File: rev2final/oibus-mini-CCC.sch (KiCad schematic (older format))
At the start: 90 parts, among them J1 Conn_01x04_Female, J2 USB_B_Micro, J3 DNP, J4 Conn_01x02_Female, P1 TC2030-MCP, Q1 DMG3415U-7, Q2 NMOS, Q3 NMOS, SW1 SW_Push, SW2 SW_Push, U1 AP2112K-3.3, U10 TPD3E001DRLR, U2 SAM-M8Q, U3 NINA-B311-00B, U4 MCP73831-2-OT, U5 MCP1624T, U6 SHT31-DIS-B, U7 DNP, U8 STM32F303CCTx, U9 DW01C-G, Y1 16M, Y2 32kHz

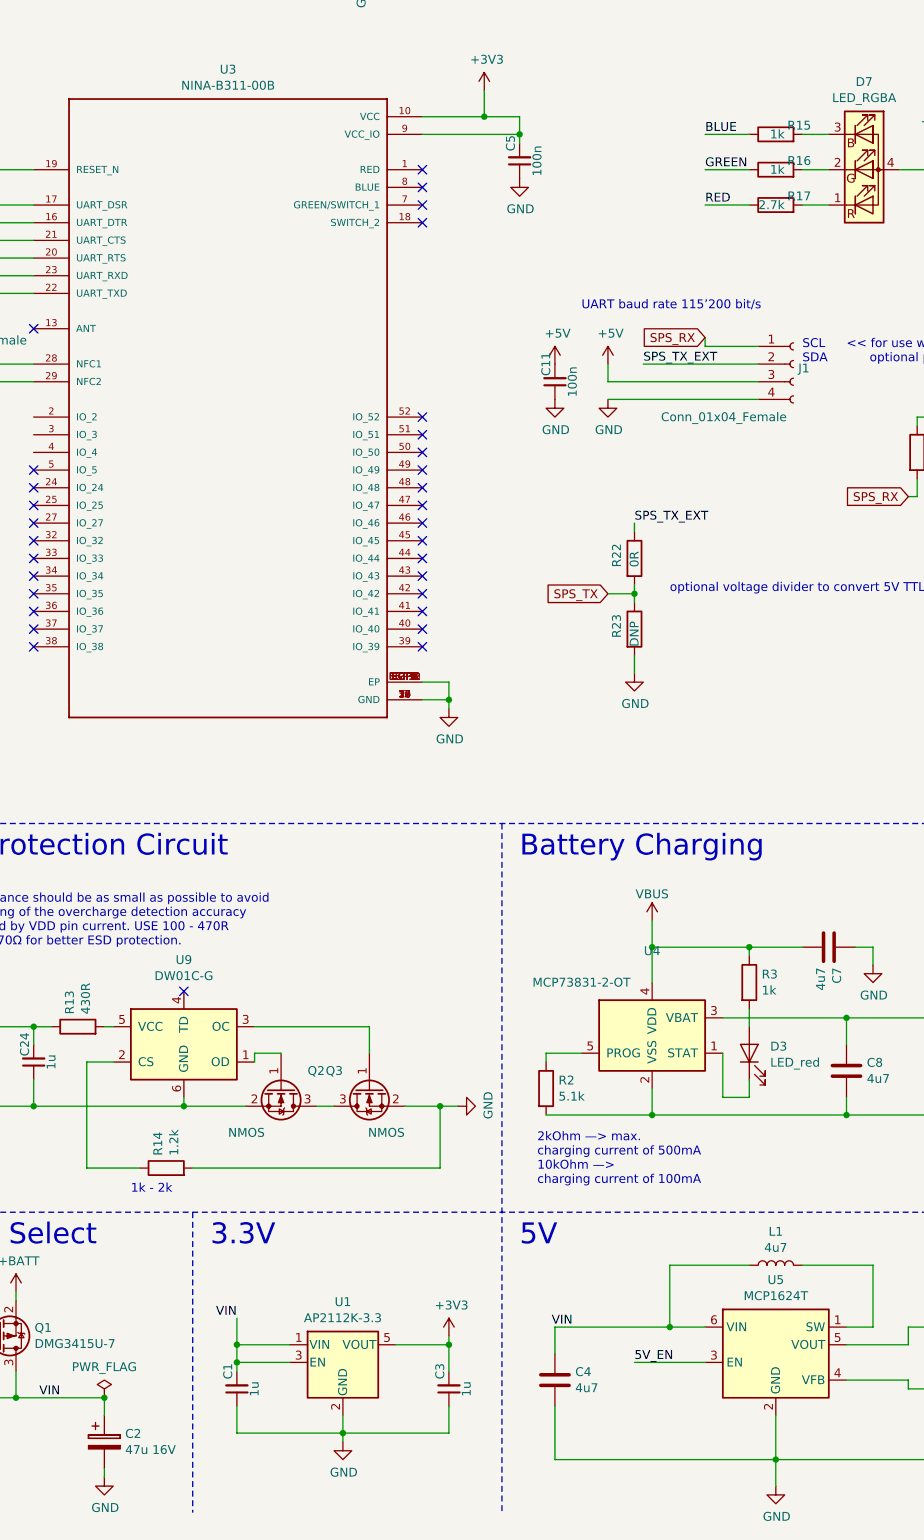
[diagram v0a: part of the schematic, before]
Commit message: Generated final Manufacturing BOM as ordered
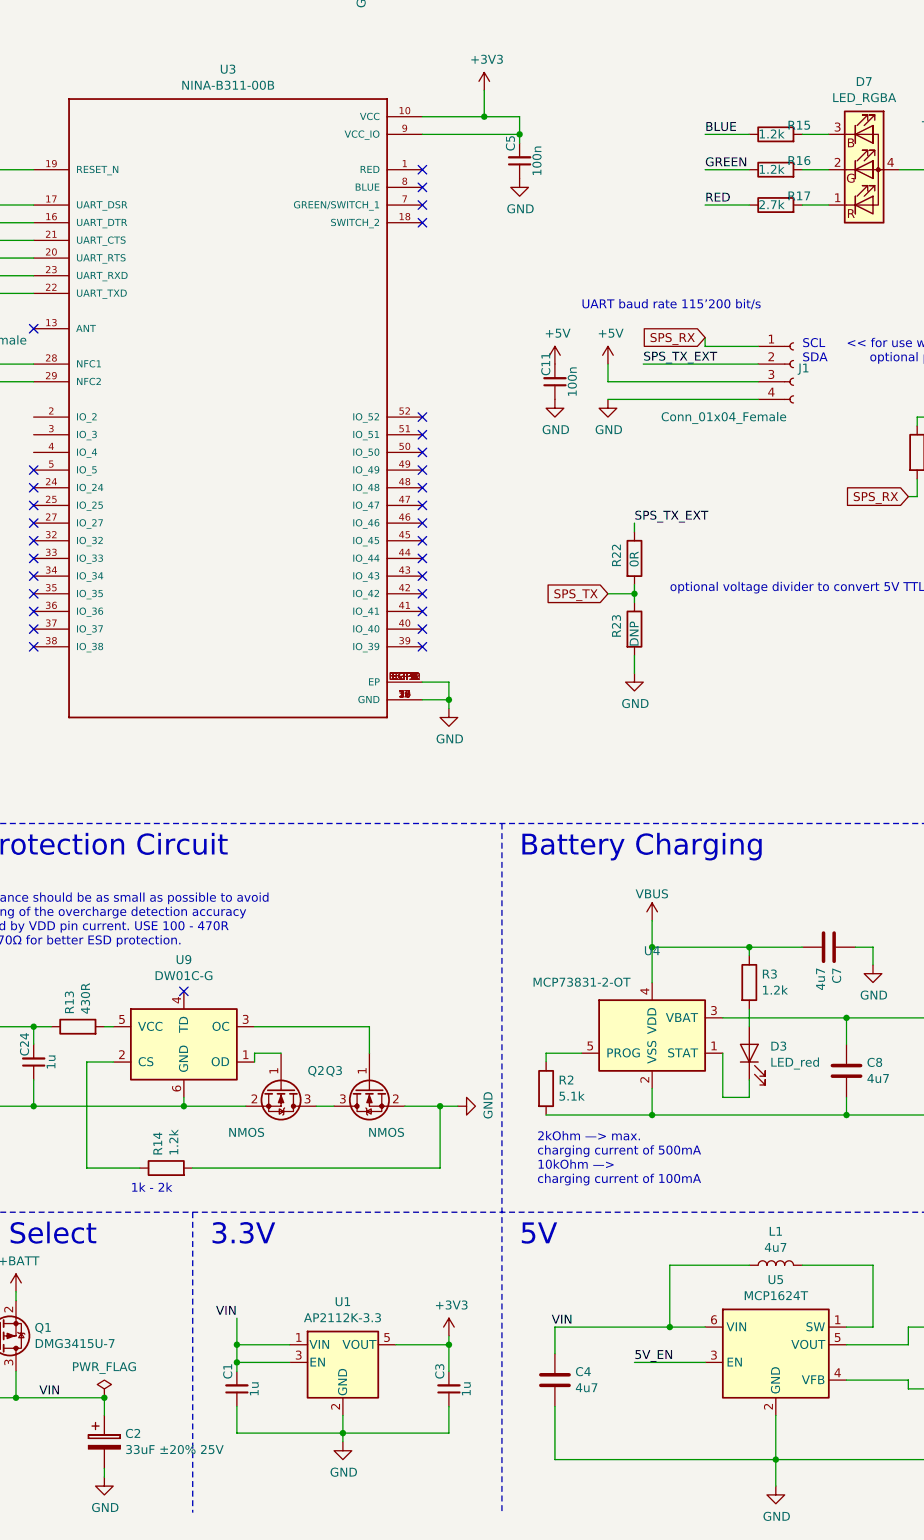
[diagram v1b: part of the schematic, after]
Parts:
- C2: value 47u 16V -> 33uF ±20% 25V; LCSC C178535 -> C336470; MPN EEEFK1C470UR -> EEEHBE330UAR
- R15, R16, R3: value 1k -> 1.2k; LCSC (none) -> C403420; MPN (none) -> ERJ3GEYJ122V
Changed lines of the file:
@@
 P 5500 8200
 F 0 "R3" H 5570 8246 50  0000 L CNN
-F 1 "1k" H 5570 8155 50  0000 L CNN
+F 1 "1.2k" H 5570 8155 50  0000 L CNN
 F 2 "Resistor_SMD:R_0603_1608Metric" V 5430 8200 50  0001 C CNN
 F 3 "~" H 5500 8200 50  0001 C CNN
+F 4 "C403420" H 5500 8200 50  0001 C CNN "LCSC"
+F 5 "ERJ3GEYJ122V" H 5500 8200 50  0001 C CNN "MPN"
 	1    5500 8200
 	1    0    0    -1
@@
 P 1850 10800
 F 0 "C2" H 1968 10846 50  0000 L CNN
-F 1 "47u 16V" H 1968 10755 50  0000 L CNN
+F 1 "33uF ±20% 25V " H 1968 10755 50  0000 L CNN
 F 2 "Capacitor_SMD:C_Elec_5x5.4" H 1888 10650 50  0001 C CNN
 F 3 "~" H 1850 10800 50  0001 C CNN
-F 4 "EEEFK1C470UR" H -100 2000 50  0001 C CNN "MPN"
-F 5 "C178535" H 0   0   50  0001 C CNN "LCSC"
+F 4 "EEEHBE330UAR" H -100 2000 50  0001 C CNN "MPN"
+F 5 "C336470" H 0   0   50  0001 C CNN "LCSC"
 	1    1850 10800
 	1    0    0    -1
@@
 P 5650 3400
 F 0 "R15" V 5700 3200 50  0000 L CNN
-F 1 "1k" V 5650 3350 50  0000 L CNN
+F 1 "1.2k" V 5650 3350 50  0000 L CNN
 F 2 "Resistor_SMD:R_0603_1608Metric" V 5580 3400 50  0001 C CNN
 F 3 "~" H 5650 3400 50  0001 C CNN
-F 4 "" H -9000 200 50  0001 C CNN "MPN"
+F 4 "ERJ3GEYJ122V" H -9000 200 50  0001 C CNN "MPN"
+F 5 "C403420" H 5650 3400 50  0001 C CNN "LCSC"
 	1    5650 3400
 	0    -1   -1   0
@@
 P 5650 3600
 F 0 "R16" V 5700 3400 50  0000 L CNN
-F 1 "1k" V 5650 3550 50  0000 L CNN
+F 1 "1.2k" V 5650 3550 50  0000 L CNN
 F 2 "Resistor_SMD:R_0603_1608Metric" V 5580 3600 50  0001 C CNN
 F 3 "~" H 5650 3600 50  0001 C CNN
-F 4 "" H -9000 400 50  0001 C CNN "MPN"
+F 4 "ERJ3GEYJ122V" H -9000 400 50  0001 C CNN "MPN"
+F 5 "C403420" H 5650 3600 50  0001 C CNN "LCSC"
 	1    5650 3600
 	0    -1   -1   0

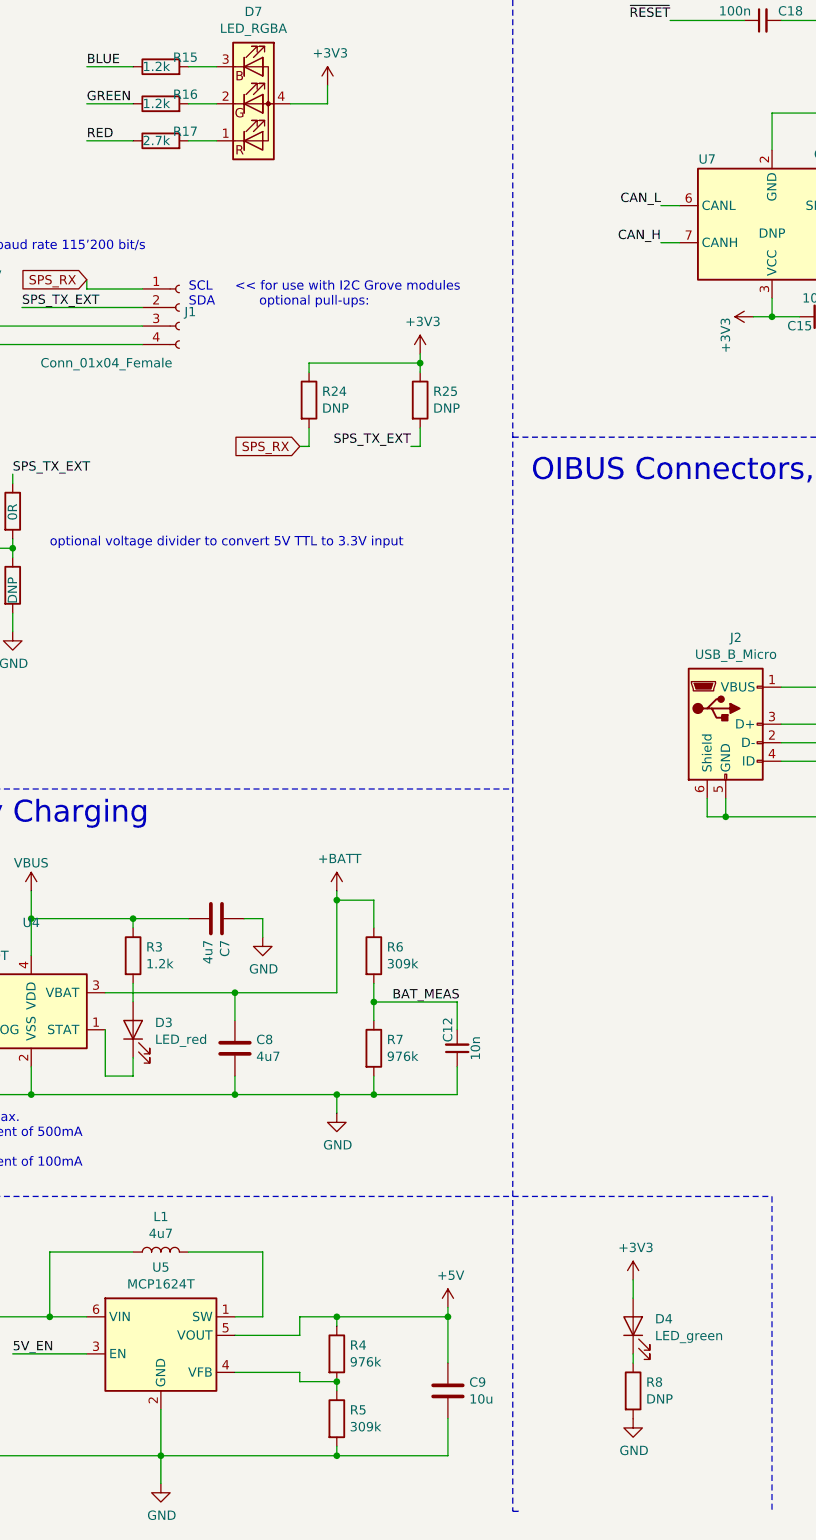
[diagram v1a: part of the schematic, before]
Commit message: added final BOM with proven parts values; de-cluttered repository; generated HTML BOM
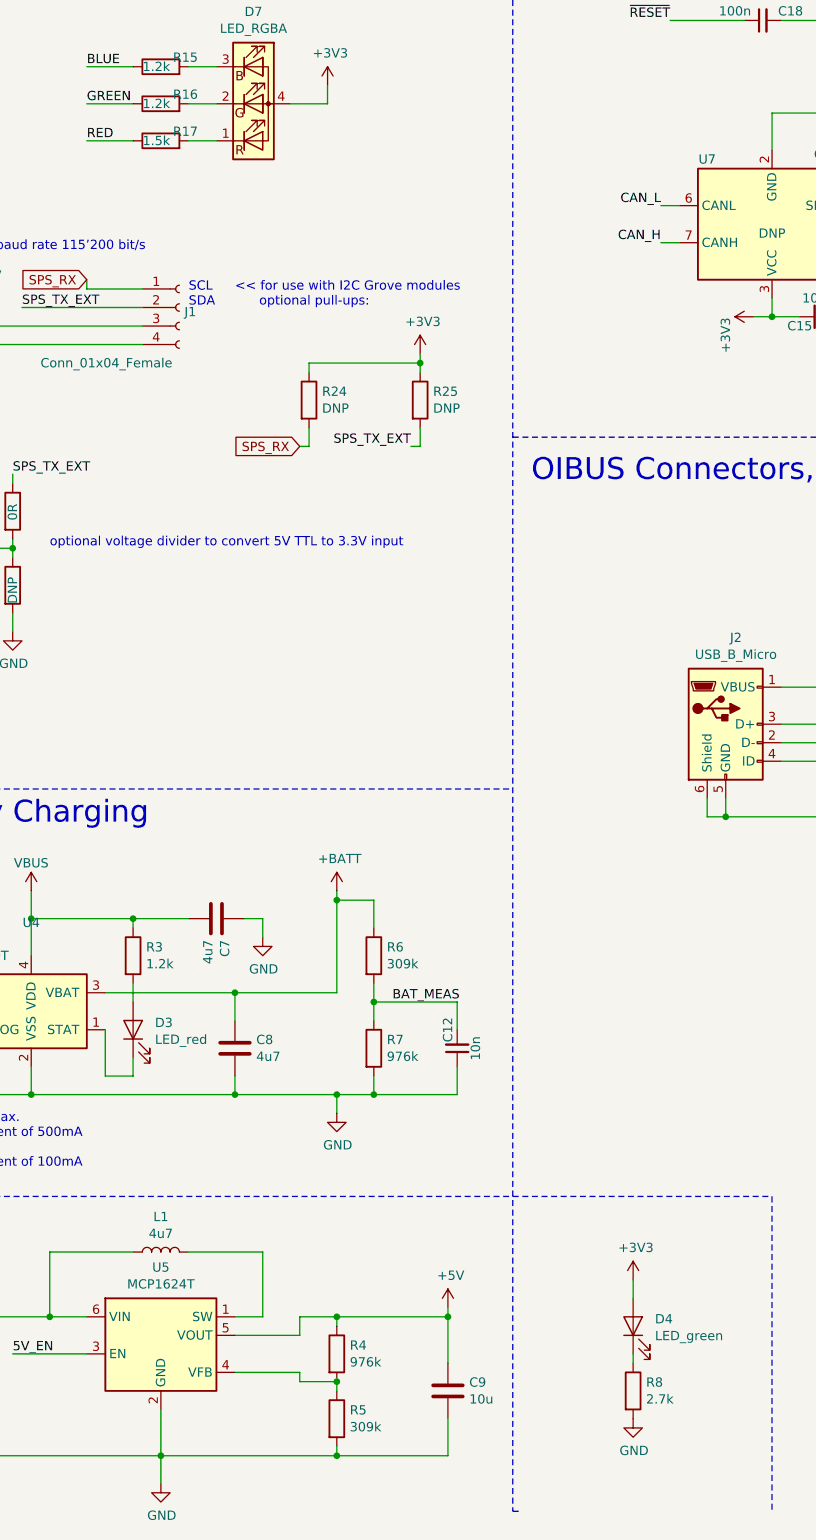
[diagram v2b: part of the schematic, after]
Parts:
- R17: value 2.7k -> 1.5k; LCSC C144097 -> (none); MPN AF0603FR-072K7L -> (none)
- R8: value DNP -> 2.7k; LCSC (none) -> C144097; MPN (none) -> AF0603FR-072K7L
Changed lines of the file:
@@
 P 8200 10550
 F 0 "R8" H 8270 10596 50  0000 L CNN
-F 1 "DNP" H 8270 10505 50  0000 L CNN
+F 1 "2.7k" H 8270 10505 50  0000 L CNN
 F 2 "Resistor_SMD:R_0603_1608Metric" V 8130 10550 50  0001 C CNN
 F 3 "~" H 8200 10550 50  0001 C CNN
+F 4 "C144097" H 8200 10550 50  0001 C CNN "LCSC"
+F 5 "AF0603FR-072K7L" H 8200 10550 50  0001 C CNN "MPN"
 	1    8200 10550
 	1    0    0    -1
@@
 P 5650 3800
 F 0 "R17" V 5700 3600 50  0000 L CNN
-F 1 "2.7k" V 5650 3750 50  0000 L CNN
+F 1 "1.5k" V 5650 3750 50  0000 L CNN
 F 2 "Resistor_SMD:R_0603_1608Metric" V 5580 3800 50  0001 C CNN
 F 3 "~" H 5650 3800 50  0001 C CNN
-F 4 "AF0603FR-072K7L" H -9000 600 50  0001 C CNN "MPN"
-F 5 "C144097" H 5650 3800 50  0001 C CNN "LCSC"
+F 4 "" H -9000 600 50  0001 C CNN "MPN"
+F 5 "" H 5650 3800 50  0001 C CNN "LCSC"
 	1    5650 3800
 	0    -1   -1   0
